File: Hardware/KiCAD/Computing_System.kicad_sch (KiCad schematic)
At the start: 6 parts, among them J1 SD_Card, U1 ESP32-C3-WROOM-02

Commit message: Added components for amplifier, RF switch, 5v Boost, renamed footprints
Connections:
- net +3.3V renamed 3V3_Computing_Power
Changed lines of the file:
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@@
-    (stroke (width 0) (type default))
-  )
-  (wire (pts (xy 200.66 46.99) (xy 200.66 44.45))
     (stroke (width 0) (type default))
   )
@@
     (stroke (width 0) (type default))
   )
-  (wire (pts (xy 196.85 45.72) (xy 196.85 46.99))
-    (stroke (width 0) (type default))
-  )
   (wire (pts (xy 191.77 49.53) (xy 191.77 58.42))
     (stroke (width 0) (type default))
@@
     (stroke (width 0) (type default))
   )
+  (wire (pts (xy 187.96 34.29) (xy 187.96 44.45))
+    (stroke (width 0) (type default))
+  )
   (wire (pts (xy 180.34 64.77) (xy 180.34 90.17))
     (stroke (width 0) (type default))
@@
     (stroke (width 0) (type default))
   )
-  (wire (pts (xy 200.66 44.45) (xy 218.44 44.45))
-    (stroke (width 0) (type default))
-  )
   (wire (pts (xy 218.44 41.91) (xy 191.77 41.91))
     (stroke (width 0) (type default))
@@
     (stroke (width 0) (type default))
   )
+  (wire (pts (xy 187.96 44.45) (xy 218.44 44.45))
+    (stroke (width 0) (type default))
+  )
   (wire (pts (xy 114.3 48.26) (xy 111.76 48.26))
     (stroke (width 0) (type default))
@@
   )
   (wire (pts (xy 119.38 39.37) (xy 121.92 39.37))
-    (stroke (width 0) (type default))
-  )
-  (wire (pts (xy 196.85 46.99) (xy 200.66 46.99))
     (stroke (width 0) (type default))
   )
@@
     (effects (font (size 1.27 1.27)) (justify left))
   )
+  (hierarchical_label "3V3_Computing_Power" (shape input) (at 187.96 34.29 0) (fields_autoplaced)
+    (effects (font (size 1.27 1.27)) (justify left))
+  )
   (hierarchical_label "CC_SCLK" (shape output) (at 182.88 90.17 0) (fields_autoplaced)
     (effects (font (size 1.27 1.27)) (justify left))
@@
     (effects (font (size 1.27 1.27)) (justify left))
   )
-  (symbol (lib_id "power:+3.3V") (at 121.92 36.83 0) (unit 1)
-    (in_bom yes) (on_board yes) (dnp no) (fields_autoplaced)
-    (property "Reference" "#PWR025" (at 121.92 40.64 0)
-      (effects (font (size 1.27 1.27)) hide)
-    )
-    (property "Value" "+3.3V" (at 121.92 31.75 0)
-      (effects (font (size 1.27 1.27)))
-    )
-    (property "Footprint" "" (at 121.92 36.83 0)
-      (effects (font (size 1.27 1.27)) hide)
-    )
-    (property "Datasheet" "" (at 121.92 36.83 0)
-      (effects (font (size 1.27 1.27)) hide)
-    )
-    (pin "1")
-    (instances
-      (project "Cobalt-Cowboy"
-        (path "/60a68eb1-aa0f-414e-b03b-965ad6b52dab/1039084b-a0e1-47ac-823b-a237cfc3ed39"
-          (reference "#PWR025") (unit 1)
-        )
-      )
-    )
+  (hierarchical_label "3V3_Computing_Power" (shape input) (at 121.92 36.83 0) (fields_autoplaced)
+    (effects (font (size 1.27 1.27)) (justify left))
   )
   (symbol (lib_id "Connector:SD_Card") (at 241.3 44.45 0) (unit 1)
@@
         )
       )
-    )
-  )
-  (symbol (lib_id "power:+3.3V") (at 196.85 45.72 0) (unit 1)
-    (in_bom yes) (on_board yes) (dnp no) (fields_autoplaced)
-    (property "Reference" "#PWR037" (at 196.85 49.53 0)
-      (effects (font (size 1.27 1.27)) hide)
-    )
-    (property "Value" "+3.3V" (at 196.85 40.64 0)
-      (effects (font (size 1.27 1.27)))
-    )
-    (property "Footprint" "" (at 196.85 45.72 0)
-      (effects (font (size 1.27 1.27)) hide)
-    )
-    (property "Datasheet" "" (at 196.85 45.72 0)
-      (effects (font (size 1.27 1.27)) hide)
-    )
-    (pin "1")
-    (instances
-      (project "Cobalt-Cowboy"
-        (path "/60a68eb1-aa0f-414e-b03b-965ad6b52dab/1039084b-a0e1-47ac-823b-a237cfc3ed39"
-          (reference "#PWR037") (unit 1)
-        )
-      )

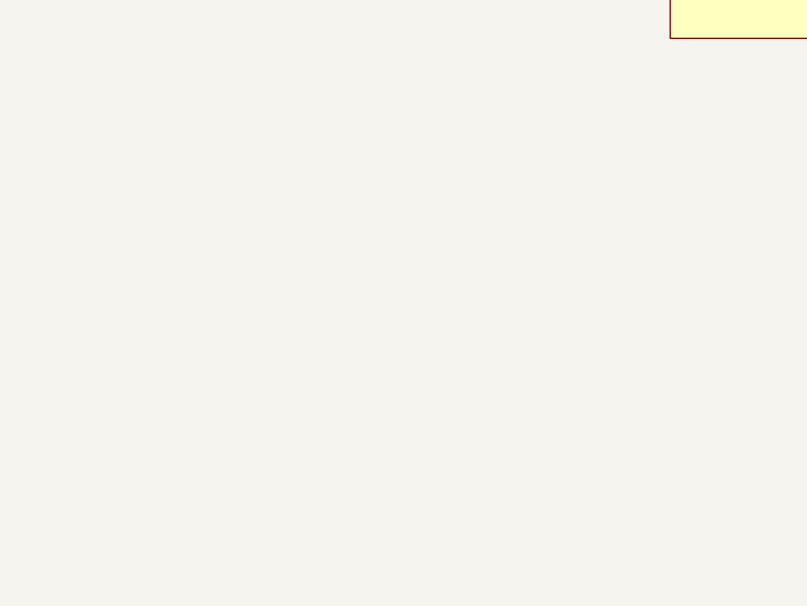
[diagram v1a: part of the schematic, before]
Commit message: added  keypad
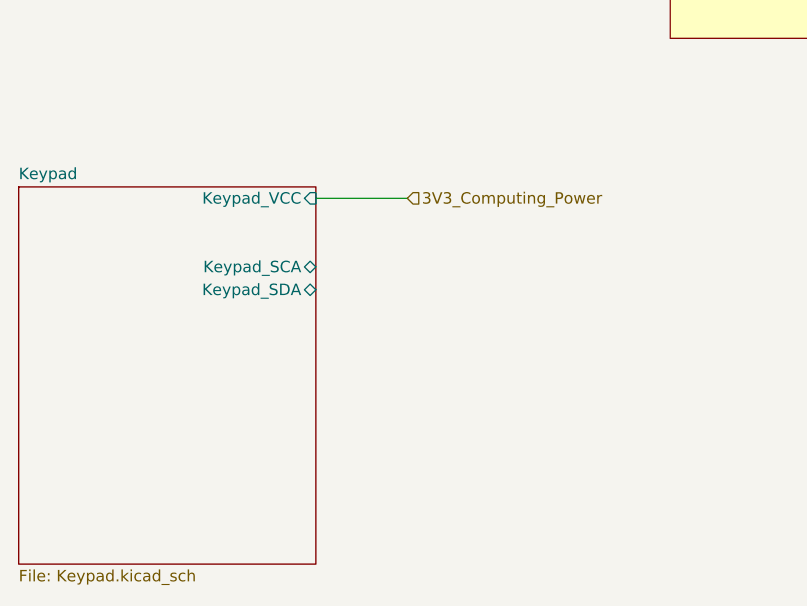
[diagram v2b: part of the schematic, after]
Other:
- added sheet Keypad (Keypad.kicad_sch)
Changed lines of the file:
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@@
+    (stroke (width 0) (type default))
+  )
+  (wire (pts (xy 57.15 113.03) (xy 67.31 113.03))
     (stroke (width 0) (type default))
   )
@@
   )
   (hierarchical_label "ESP32_USB_DN" (shape bidirectional) (at 157.48 64.77 0) (fields_autoplaced)
+    (effects (font (size 1.27 1.27)) (justify left))
+  )
+  (hierarchical_label "3V3_Computing_Power" (shape input) (at 67.31 113.03 0) (fields_autoplaced)
     (effects (font (size 1.27 1.27)) (justify left))
   )
@@
       )
     )
+  )
+  (sheet (at 24.13 111.76) (size 33.02 41.91) (fields_autoplaced)
+    (stroke (width 0.1524) (type solid))
+    (fill (color 0 0 0 0.0000))
+    (property "Sheetname" "Keypad" (at 24.13 111.0484 0)
+      (effects (font (size 1.27 1.27)) (justify left bottom))
+    )
+    (property "Sheetfile" "Keypad.kicad_sch" (at 24.13 154.2546 0)
+      (effects (font (size 1.27 1.27)) (justify left top))
+    )
+    (pin "Keypad_SCA" bidirectional (at 57.15 120.65 0)
+      (effects (font (size 1.27 1.27)) (justify right))
+    )
+    (pin "Keypad_SDA" bidirectional (at 57.15 123.19 0)
+      (effects (font (size 1.27 1.27)) (justify right))
+    )
+    (pin "Keypad_VCC" input (at 57.15 113.03 0)
+      (effects (font (size 1.27 1.27)) (justify right))
+    )
+    (instances
+      (project "Cobalt-Cowboy"
+        (path "/60a68eb1-aa0f-414e-b03b-965ad6b52dab/1039084b-a0e1-47ac-823b-a237cfc3ed39" (page "6"))
+      )
+    )

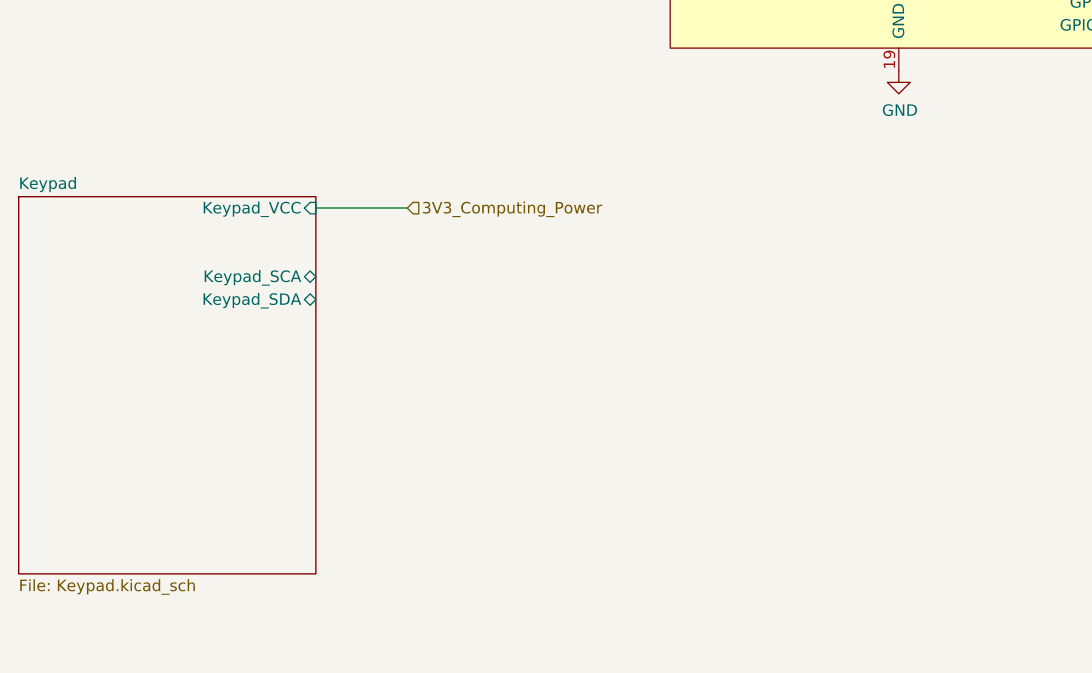
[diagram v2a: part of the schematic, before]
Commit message: Changed Keypad to better accomidate use of GPIO and removed inc symbols
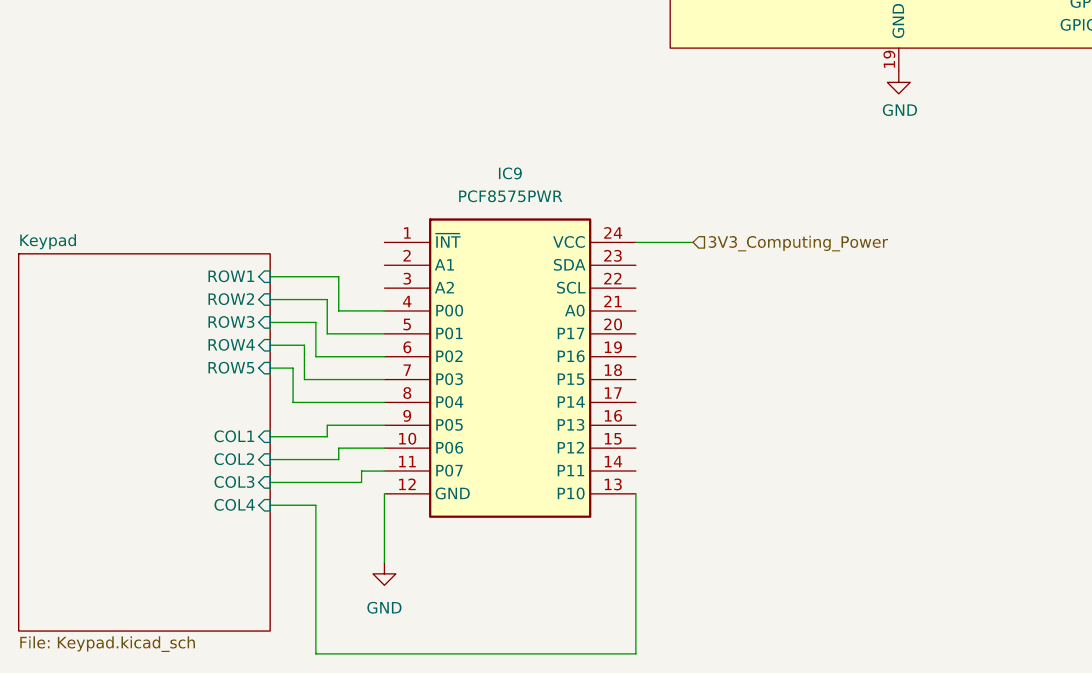
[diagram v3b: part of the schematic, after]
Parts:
- added IC9: PCF8575PWR, Cobalt_Cowboy:SOP65P640X120-24N_PCF8575PWR, symbol Cobalt-Cowboy:PCF8575PWR
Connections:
- net 3V3_Computing_Power: now also IC9.24 (VCC)
- net GND: now also IC9.12 (GND)
- new net Keypad/COL1: IC9.9 (P05)
- new net Keypad/COL2: IC9.10 (P06)
- new net Keypad/COL3: IC9.11 (P07)
- new net Keypad/COL4: IC9.13 (P10)
- new net Keypad/ROW1: IC9.4 (P00)
- new net Keypad/ROW2: IC9.5 (P01)
- new net Keypad/ROW3: IC9.6 (P02)
- new net Keypad/ROW4: IC9.7 (P03)
- new net Keypad/ROW5: IC9.8 (P04)
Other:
- sheet Keypad ports: added COL1, COL2, COL3, COL4, ROW1, ROW2, ROW3, ROW4, ROW5; removed Keypad_SCA, Keypad_SDA, Keypad_VCC

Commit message: Added seperate schematic for amplifier assembly
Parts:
- renumbered C12 to C28, C12 to C29, C12 to C30, R1 to R3
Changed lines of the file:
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@@
   (symbol (lib_id "pkl_device:pkl_C_Small") (at 116.84 48.26 90) (unit 1)
     (in_bom yes) (on_board yes) (dnp no)
-    (property "Reference" "C12" (at 115.6716 45.9232 0)
+    (property "Reference" "C29" (at 115.6716 45.9232 0)
       (effects (font (size 1.27 1.27)) (justify left))
     )
@@
     (instances
       (project "Cobalt-Cowboy"
-        (path "/60a68eb1-aa0f-414e-b03b-965ad6b52dab/d80d452c-0cd9-4253-b692-c2cdb4b1394b"
-          (reference "C12") (unit 1)
-        )
         (path "/60a68eb1-aa0f-414e-b03b-965ad6b52dab/1039084b-a0e1-47ac-823b-a237cfc3ed39"
           (reference "C29") (unit 1)
@@
   (symbol (lib_id "pkl_device:pkl_C_Small") (at 116.84 39.37 90) (unit 1)
     (in_bom yes) (on_board yes) (dnp no)
-    (property "Reference" "C12" (at 115.6716 37.0332 0)
+    (property "Reference" "C30" (at 115.6716 37.0332 0)
       (effects (font (size 1.27 1.27)) (justify left))
     )
@@
     (instances
       (project "Cobalt-Cowboy"
-        (path "/60a68eb1-aa0f-414e-b03b-965ad6b52dab/d80d452c-0cd9-4253-b692-c2cdb4b1394b"
-          (reference "C12") (unit 1)
-        )
         (path "/60a68eb1-aa0f-414e-b03b-965ad6b52dab/1039084b-a0e1-47ac-823b-a237cfc3ed39"
           (reference "C30") (unit 1)
@@
   (symbol (lib_id "power:GND") (at 191.77 58.42 0) (unit 1)
     (in_bom yes) (on_board yes) (dnp no)
-    (property "Reference" "#PWR017" (at 191.77 64.77 0)
+    (property "Reference" "#PWR038" (at 191.77 64.77 0)
       (effects (font (size 1.27 1.27)) hide)
     )
@@
     (instances
       (project "Cobalt-Cowboy"
-        (path "/60a68eb1-aa0f-414e-b03b-965ad6b52dab/d80d452c-0cd9-4253-b692-c2cdb4b1394b"
-          (reference "#PWR017") (unit 1)
-        )
         (path "/60a68eb1-aa0f-414e-b03b-965ad6b52dab/1039084b-a0e1-47ac-823b-a237cfc3ed39"
           (reference "#PWR038") (unit 1)
@@
   (symbol (lib_id "pkl_device:pkl_C_Small") (at 81.28 57.15 90) (unit 1)
     (in_bom yes) (on_board yes) (dnp no)
-    (property "Reference" "C12" (at 80.1116 54.8132 0)
+    (property "Reference" "C28" (at 80.1116 54.8132 0)
       (effects (font (size 1.27 1.27)) (justify left))
     )
@@
     (instances
       (project "Cobalt-Cowboy"
-        (path "/60a68eb1-aa0f-414e-b03b-965ad6b52dab/d80d452c-0cd9-4253-b692-c2cdb4b1394b"
-          (reference "C12") (unit 1)
-        )
         (path "/60a68eb1-aa0f-414e-b03b-965ad6b52dab/1039084b-a0e1-47ac-823b-a237cfc3ed39"
           (reference "C28") (unit 1)
@@
   (symbol (lib_id "pkl_device:pkl_R_Small") (at 91.44 50.8 90) (unit 1)
     (in_bom yes) (on_board yes) (dnp no)
-    (property "Reference" "R1" (at 95.25 52.324 90)
+    (property "Reference" "R3" (at 95.25 52.324 90)
       (effects (font (size 1.27 1.27)))
     )
@@
     (instances
       (project "Cobalt-Cowboy"
-        (path "/60a68eb1-aa0f-414e-b03b-965ad6b52dab/d80d452c-0cd9-4253-b692-c2cdb4b1394b"
-          (reference "R1") (unit 1)
-        )
         (path "/60a68eb1-aa0f-414e-b03b-965ad6b52dab/1039084b-a0e1-47ac-823b-a237cfc3ed39"
           (reference "R3") (unit 1)
@@
     (instances
       (project "Cobalt-Cowboy"
-        (path "/60a68eb1-aa0f-414e-b03b-965ad6b52dab/1039084b-a0e1-47ac-823b-a237cfc3ed39/36b248bc-2a23-4171-b336-2df6d7e58962"
+        (path "/60a68eb1-aa0f-414e-b03b-965ad6b52dab/1039084b-a0e1-47ac-823b-a237cfc3ed39"
           (reference "#PWR03") (unit 1)
         )
-        (path "/60a68eb1-aa0f-414e-b03b-965ad6b52dab/1039084b-a0e1-47ac-823b-a237cfc3ed39"
-          (reference "#PWR03") (unit 1)
-        )
       )
     )
@@
   (symbol (lib_id "power:GND") (at 76.2 59.69 0) (unit 1)
     (in_bom yes) (on_board yes) (dnp no)
-    (property "Reference" "#PWR016" (at 76.2 66.04 0)
+    (property "Reference" "#PWR041" (at 76.2 66.04 0)
       (effects (font (size 1.27 1.27)) hide)
     )
@@
     (instances
       (project "Cobalt-Cowboy"
-        (path "/60a68eb1-aa0f-414e-b03b-965ad6b52dab/d80d452c-0cd9-4253-b692-c2cdb4b1394b"
-          (reference "#PWR016") (unit 1)
-        )
         (path "/60a68eb1-aa0f-414e-b03b-965ad6b52dab/1039084b-a0e1-47ac-823b-a237cfc3ed39"
           (reference "#PWR041") (unit 1)
@@
   (symbol (lib_id "power:GND") (at 121.92 97.79 0) (unit 1)
     (in_bom yes) (on_board yes) (dnp no)
-    (property "Reference" "#PWR017" (at 121.92 104.14 0)
+    (property "Reference" "#PWR026" (at 121.92 104.14 0)
       (effects (font (size 1.27 1.27)) hide)
     )
@@
     (instances
       (project "Cobalt-Cowboy"
-        (path "/60a68eb1-aa0f-414e-b03b-965ad6b52dab/d80d452c-0cd9-4253-b692-c2cdb4b1394b"
-          (reference "#PWR017") (unit 1)
-        )
         (path "/60a68eb1-aa0f-414e-b03b-965ad6b52dab/1039084b-a0e1-47ac-823b-a237cfc3ed39"
           (reference "#PWR026") (unit 1)
@@
     (instances
       (project "Cobalt-Cowboy"
-        (path "/60a68eb1-aa0f-414e-b03b-965ad6b52dab/1039084b-a0e1-47ac-823b-a237cfc3ed39/36b248bc-2a23-4171-b336-2df6d7e58962"
+        (path "/60a68eb1-aa0f-414e-b03b-965ad6b52dab/1039084b-a0e1-47ac-823b-a237cfc3ed39"
           (reference "IC9") (unit 1)
-        )
-        (path "/60a68eb1-aa0f-414e-b03b-965ad6b52dab/1039084b-a0e1-47ac-823b-a237cfc3ed39"
-          (reference "IC9") (unit 1)
